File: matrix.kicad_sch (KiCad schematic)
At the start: 1 part

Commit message: schematics
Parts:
- added SW10, SW11, SW12, SW13, SW14, SW15, SW16, SW17, SW18, SW19, SW2, SW20, SW21, SW22, SW23, SW24, SW25, SW26, SW27, SW28, SW29, SW3, SW30, SW31, SW32, SW33, SW34, SW35, SW36, SW37, SW4, SW5, SW6, SW7, SW8, SW9: EC_SW, cipulot_parts:ecs_pad_1U_no_ring, symbol cipulot_parts:EC_SW
- SW1: renamed from SW?; footprint (none) -> cipulot_parts:ecs_pad_1U_no_ring
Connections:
- net ROW0: now reaches SW1.1
- net ROW0: now also SW10.1, SW11.1, SW2.1, SW3.1, SW4.1, SW5.1, SW6.1, SW7.1, SW8.1, SW9.1
- net COL0: now reaches SW1.2
- net COL0: now also SW12.2, SW22.2
- net GND: now reaches SW1.3 (SG)
- net GND: now also SW10.3 (SG), SW11.3 (SG), SW12.3 (SG), SW13.3 (SG), SW14.3 (SG), SW15.3 (SG), SW16.3 (SG), SW17.3 (SG), SW18.3 (SG), SW19.3 (SG), SW2.3 (SG), SW20.3 (SG), SW21.3 (SG), SW22.3 (SG), SW23.3 (SG), SW24.3 (SG), SW25.3 (SG), SW26.3 (SG), SW27.3 (SG), SW28.3 (SG), SW29.3 (SG), SW3.3 (SG), SW30.3 (SG), SW31.3 (SG), SW32.3 (SG), SW33.3 (SG), SW34.3 (SG), SW35.3 (SG), SW36.3 (SG), SW37.3 (SG), SW4.3 (SG), SW5.3 (SG), SW6.3 (SG), SW7.3 (SG), SW8.3 (SG), SW9.3 (SG)
- new net COL1: SW13.2, SW2.2, SW23.2
- new net COL10: SW11.2
- new net COL2: SW14.2, SW24.2, SW3.2, SW32.2
- new net COL3: SW15.2, SW25.2, SW33.2, SW4.2
- new net COL4: SW16.2, SW26.2, SW34.2, SW5.2
- new net COL5: SW17.2, SW27.2, SW35.2, SW6.2
- new net COL6: SW18.2, SW28.2, SW36.2, SW7.2
- new net COL7: SW19.2, SW29.2, SW37.2, SW8.2
- new net COL8: SW20.2, SW30.2, SW9.2
- new net COL9: SW10.2, SW21.2, SW31.2
- new net ROW1: SW12.1, SW13.1, SW14.1, SW15.1, SW16.1, SW17.1, SW18.1, SW19.1, SW20.1, SW21.1
- new net ROW2: SW22.1, SW23.1, SW24.1, SW25.1, SW26.1, SW27.1, SW28.1, SW29.1, SW30.1, SW31.1
- new net ROW3: SW32.1, SW33.1, SW34.1, SW35.1, SW36.1, SW37.1
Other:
- moved on the sheet: SW1

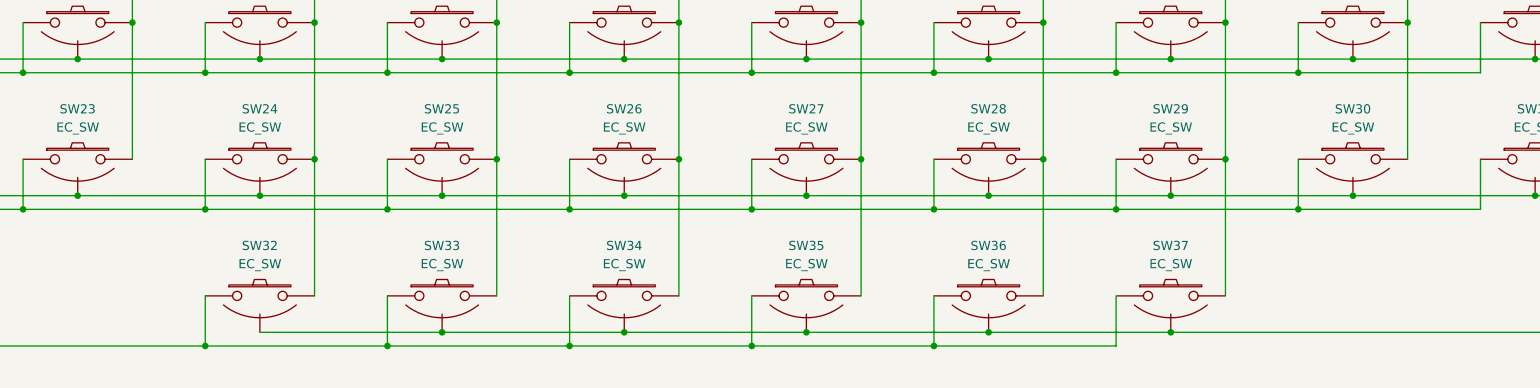
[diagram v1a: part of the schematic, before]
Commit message: changed rol, col schematics /// made pcb 4 layers
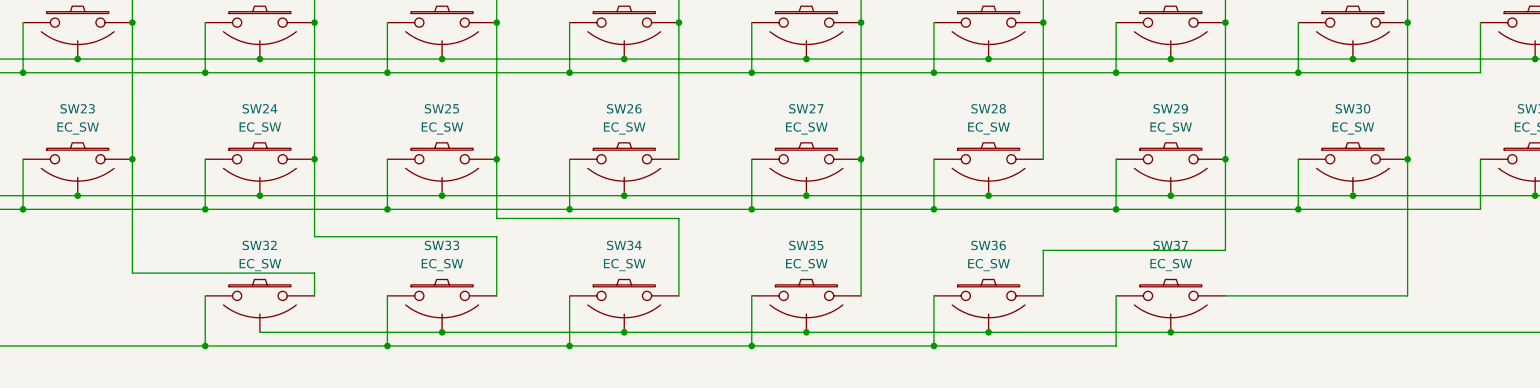
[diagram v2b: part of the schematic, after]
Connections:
- net COL1: now also SW32.2
- net COL2: now also SW33.2; no longer SW32.2
- net COL3: now also SW34.2; no longer SW33.2
- net COL4: no longer SW34.2
- net COL6: no longer SW36.2
- net COL7: now also SW36.2; no longer SW37.2
- net COL8: now also SW37.2

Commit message: early routing
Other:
- note added: "CHANGE COL 10!?!?!?!!?"
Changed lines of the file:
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@@
     (stroke (width 0) (type default) (color 0 0 0 0))
+  )
+  (text "CHANGE COL 10!?!?!?!!?" (at 318.135 78.74 0)
+    (effects (font (size 4 4)) (justify left bottom))
   )
   (global_label "ROW3" (shape input) (at 73.025 168.91 180) (fields_autoplaced)

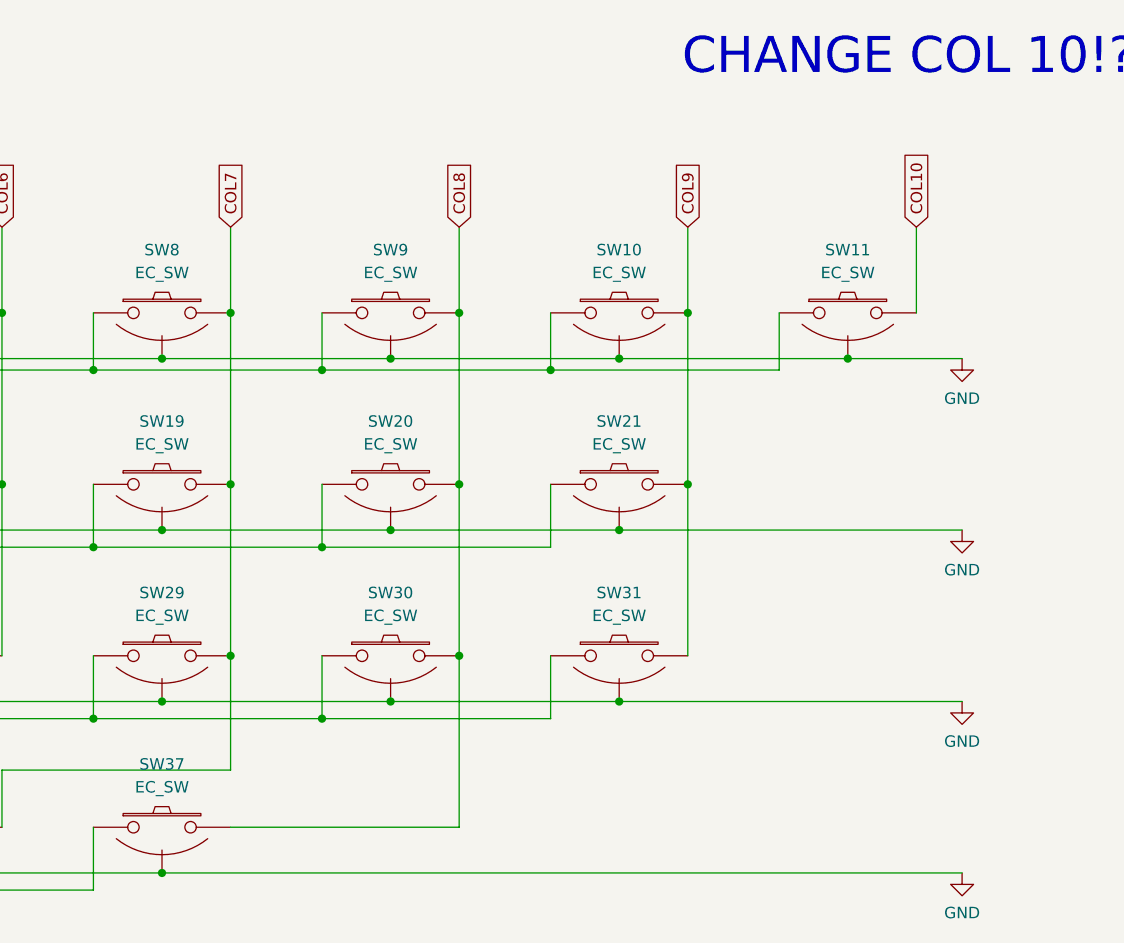
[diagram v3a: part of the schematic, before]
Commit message: component placement
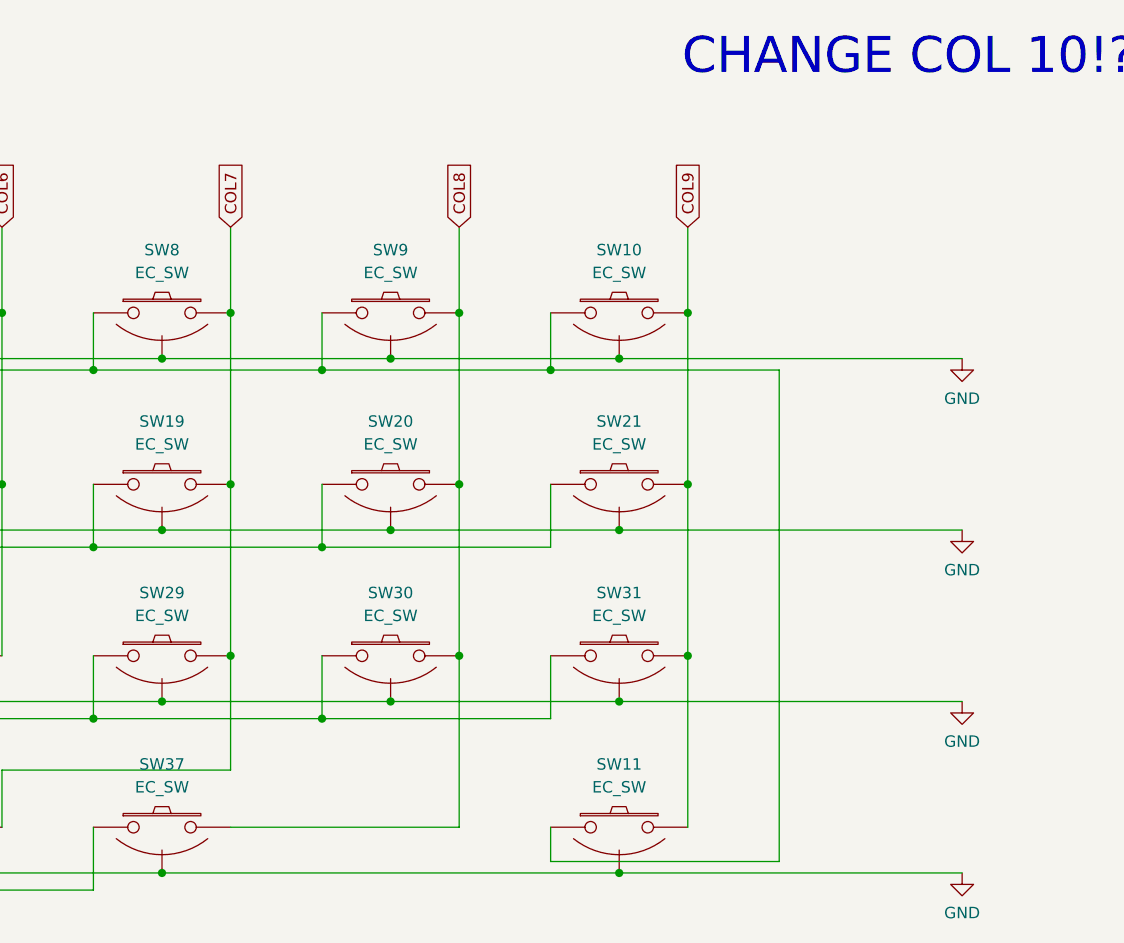
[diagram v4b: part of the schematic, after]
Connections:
- net COL10 is gone; now on net COL9: SW11.2
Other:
- moved on the sheet: SW11
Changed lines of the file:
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@@
   (junction (at 260.35 128.905) (diameter 0) (color 0 0 0 0)
   )
-  (junction (at 336.55 109.855) (diameter 0) (color 0 0 0 0)
+  (junction (at 311.15 167.005) (diameter 0) (color 0 0 0 0)
   )
   (junction (at 311.15 109.855) (diameter 0) (color 0 0 0 0)
@@
   (junction (at 74.93 149.86) (diameter 0) (color 0 0 0 0)
   )
+  (junction (at 318.77 142.875) (diameter 0) (color 0 0 0 0)
+  )
   (junction (at 209.55 109.855) (diameter 0) (color 0 0 0 0)
   )
@@
     (stroke (width 0) (type default) (color 0 0 0 0))
   )
-  (wire (pts (xy 328.93 104.775) (xy 328.93 111.125))
-    (stroke (width 0) (type default) (color 0 0 0 0))
-  )
   (wire (pts (xy 227.33 161.925) (xy 227.33 168.91))
     (stroke (width 0) (type default) (color 0 0 0 0))
@@
     (stroke (width 0) (type default) (color 0 0 0 0))
   )
+  (wire (pts (xy 318.77 142.875) (xy 318.77 161.925))
+    (stroke (width 0) (type default) (color 0 0 0 0))
+  )
   (wire (pts (xy 201.93 104.775) (xy 201.93 111.125))
     (stroke (width 0) (type default) (color 0 0 0 0))
@@
     (stroke (width 0) (type default) (color 0 0 0 0))
   )
+  (wire (pts (xy 303.53 161.925) (xy 303.53 165.735))
+    (stroke (width 0) (type default) (color 0 0 0 0))
+  )
   (wire (pts (xy 201.93 168.91) (xy 176.53 168.91))
     (stroke (width 0) (type default) (color 0 0 0 0))
@@
     (stroke (width 0) (type default) (color 0 0 0 0))
   )
-  (wire (pts (xy 336.55 109.855) (xy 349.25 109.855))
+  (wire (pts (xy 311.15 109.855) (xy 349.25 109.855))
     (stroke (width 0) (type default) (color 0 0 0 0))
   )
@@
     (stroke (width 0) (type default) (color 0 0 0 0))
   )
-  (wire (pts (xy 311.15 109.855) (xy 336.55 109.855))
-    (stroke (width 0) (type default) (color 0 0 0 0))
-  )
   (wire (pts (xy 318.77 104.775) (xy 318.77 95.25))
     (stroke (width 0) (type default) (color 0 0 0 0))
@@
     (stroke (width 0) (type default) (color 0 0 0 0))
   )
-  (wire (pts (xy 344.17 95.25) (xy 344.17 104.775))
-    (stroke (width 0) (type default) (color 0 0 0 0))
-  )
   (wire (pts (xy 227.33 104.775) (xy 227.33 111.125))
     (stroke (width 0) (type default) (color 0 0 0 0))
@@
     (stroke (width 0) (type default) (color 0 0 0 0))
   )
+  (wire (pts (xy 311.15 167.005) (xy 349.25 167.005))
+    (stroke (width 0) (type default) (color 0 0 0 0))
+  )
   (wire (pts (xy 166.37 151.13) (xy 191.77 151.13))
     (stroke (width 0) (type default) (color 0 0 0 0))
@@
     (stroke (width 0) (type default) (color 0 0 0 0))
   )
+  (wire (pts (xy 303.53 165.735) (xy 328.93 165.735))
+    (stroke (width 0) (type default) (color 0 0 0 0))
+  )
   (wire (pts (xy 140.97 95.25) (xy 140.97 104.775))
     (stroke (width 0) (type default) (color 0 0 0 0))
@@
     (stroke (width 0) (type default) (color 0 0 0 0))
   )
-  (wire (pts (xy 260.35 167.005) (xy 349.25 167.005))
+  (wire (pts (xy 260.35 167.005) (xy 311.15 167.005))
     (stroke (width 0) (type default) (color 0 0 0 0))
   )
@@
   )
   (wire (pts (xy 158.75 167.005) (xy 184.15 167.005))
+    (stroke (width 0) (type default) (color 0 0 0 0))
+  )
+  (wire (pts (xy 328.93 111.125) (xy 328.93 165.735))
     (stroke (width 0) (type default) (color 0 0 0 0))
   )
@@
     )
   )
-  (global_label "COL10" (shape input) (at 344.17 95.25 90) (fields_autoplaced)
-    (effects (font (size 1.27 1.27)) (justify left))
-    (property "Intersheet References" "${INTERSHEET_REFS}" (id 0) (at 344.0906 86.7893 90)
-      (effects (font (size 1.27 1.27)) (justify left) hide)
-    )
-  )
   (global_label "COL1" (shape input) (at 115.57 95.25 90) (fields_autoplaced)
     (effects (font (size 1.27 1.27)) (justify left))
@@
     (pin "3")
   )
-  (symbol (lib_id "cipulot_parts:EC_SW") (at 336.55 104.775 0) (unit 1)
-    (in_bom yes) (on_board yes) (fields_autoplaced)
-    (property "Reference" "SW11" (id 0) (at 336.55 97.79 0))
-    (property "Value" "EC_SW" (id 1) (at 336.55 100.33 0))
-    (property "Footprint" "cipulot_parts:ecs_pad_1U_no_ring" (id 2) (at 336.55 104.775 0)
-      (effects (font (size 1.27 1.27)) hide)
-    )
-    (property "Datasheet" "" (id 3) (at 336.55 104.775 0))
-    (pin "1")
-    (pin "2")
+  (symbol (lib_id "cipulot_parts:EC_SW") (at 311.15 161.925 0) (unit 1)
+    (in_bom yes) (on_board yes) (fields_autoplaced)
+    (property "Reference" "SW11" (id 0) (at 311.15 154.94 0))
+    (property "Value" "EC_SW" (id 1) (at 311.15 157.48 0))
+    (property "Footprint" "cipulot_parts:ecs_pad_1U_no_ring" (id 2) (at 311.15 161.925 0)
+      (effects (font (size 1.27 1.27)) hide)
+    )
+    (property "Datasheet" "" (id 3) (at 311.15 161.925 0))
+    (pin "1")
+    (pin "2")

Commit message: routing work
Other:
- note removed: "CHANGE COL 10!?!?!?!!?"
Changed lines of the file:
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@@
     (stroke (width 0) (type default) (color 0 0 0 0))
-  )
-  (text "CHANGE COL 10!?!?!?!!?" (at 318.135 78.74 0)
-    (effects (font (size 4 4)) (justify left bottom))
   )
   (global_label "ROW3" (shape input) (at 73.025 168.91 180) (fields_autoplaced)

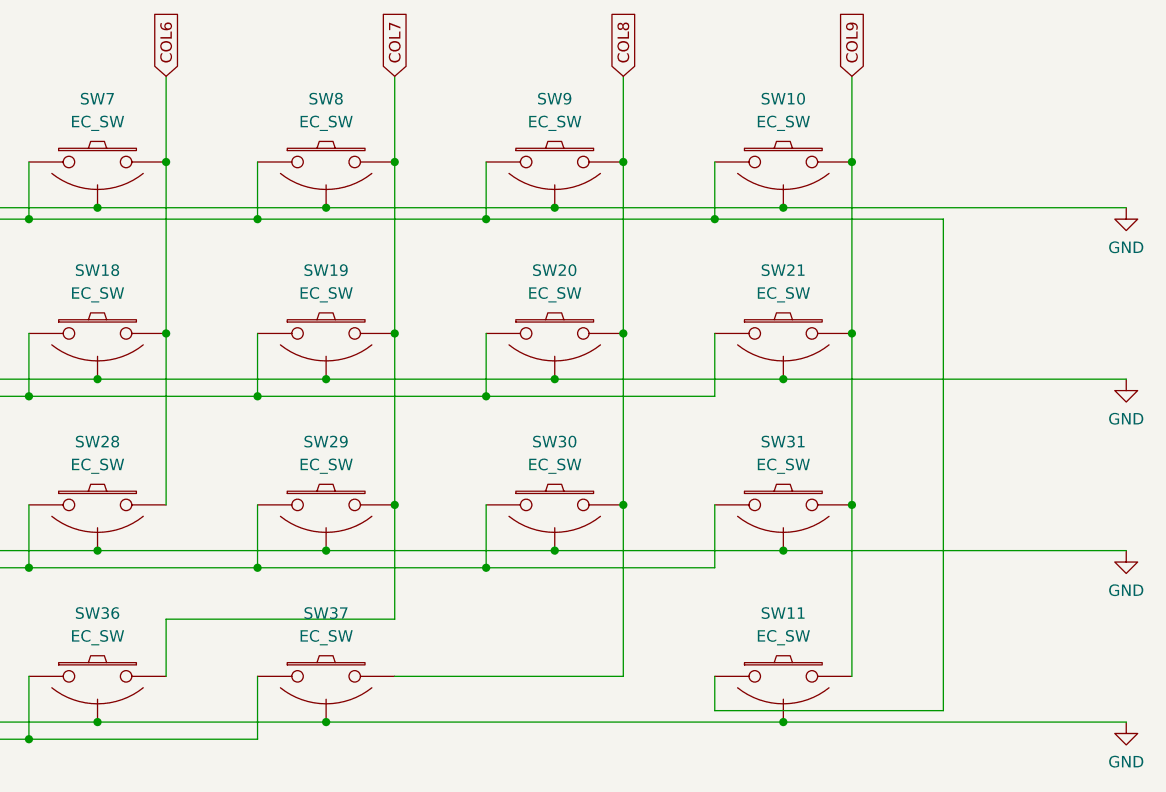
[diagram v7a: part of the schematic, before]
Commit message: rerouting matrix to fix error
shifting around a bunch of switches, ending up with hopefully functional but not pretty routing
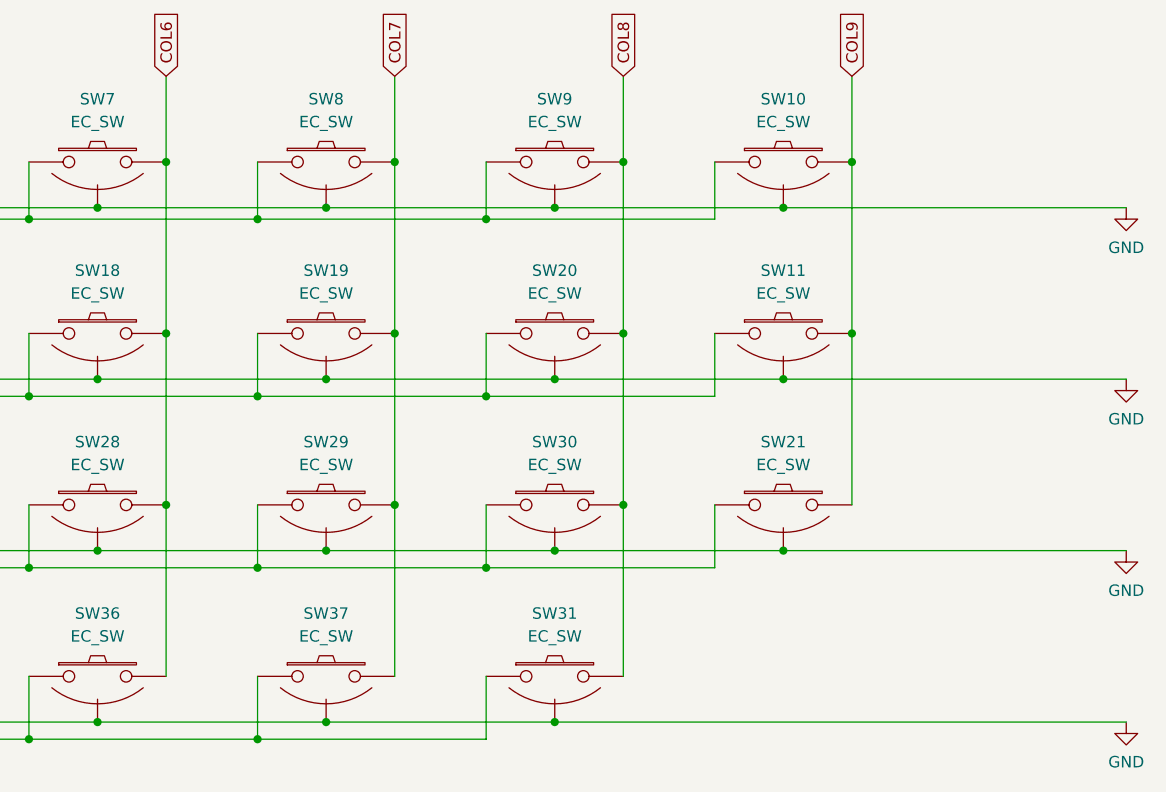
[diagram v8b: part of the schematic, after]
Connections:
- net COL6: now also SW36.2
- net COL7: now also SW37.2; no longer SW36.2
- net COL8: now also SW31.2; no longer SW37.2
- net COL9: no longer SW31.2
- net ROW0: no longer SW11.1
- net ROW1: now also SW11.1; no longer SW21.1
- net ROW2: now also SW21.1; no longer SW31.1
- net ROW3: now also SW31.1
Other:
- moved on the sheet: SW11, SW21, SW31
